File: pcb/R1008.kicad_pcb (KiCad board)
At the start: 2 copper layers, 45 x 33.3 mm, 9 parts, among them J1 PCIEXPRESS-X1, J2 CONN_R1000A_EXTENSION

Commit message: wip
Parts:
- removed G***: LOGO, pluggee:pluggee-LOGO-131X127
- removed G***: LOGO, pluggee:pluggee-QRNEG-085X085
- removed G***: LOGO, pluggee:pluggee-QRNEG-254X254
- removed MP1, MP2, MP3, MP4: ZIPTIE, Main:SLOT_ZIPTIE
- added C1: C0603, Main:CAPC0603, B.Cu at (128.2, 76.3)
- added C2: C0603, Main:CAPC0603, B.Cu at (148.2, 82.7)
- added C3: C0603, Main:CAPC0603, B.Cu at (148.2, 71.2)
- added C4: C0603, Main:CAPC0603, B.Cu at (148.2, 84.4)
- added C5: C0603, Main:CAPC0603, B.Cu at (148.2, 72.9)
- added C6: C0603, Main:CAPC0603, B.Cu at (145.0, 79.4)
- added C7: C0603, Main:CAPC0603, B.Cu at (145.0, 90.9)
- added J3: SOCKET254P-01X04-1725672, Main:SOCKET254P-01X04-1725672, B.Cu at (163.0, 76.0)
- added J4: CONN_01X03, Main:SOCKET254P-01X03, B.Cu at (152.5, 74.7)
- added J5: CONN_01X04, Main:SOCKET254P-01X04, B.Cu at (157.0, 76.0)
- added J6: CONN_01X03, Main:SOCKET254P-01X03, B.Cu at (152.5, 86.2)
- added J7: CONN_01X04, Main:SOCKET254P-01X04, B.Cu at (157.0, 87.5)
- added J8: CONN_01X03, Main:SOCKET254P-01X03, B.Cu at (131.3, 71.9)
- added R1: R0603, Main:RESC0603, B.Cu at (127.7, 92.4)
- added R10: R1206, Main:RESC1206, B.Cu at (148.2, 87.5)
- added R11: R0603, Main:RESC0603, B.Cu at (127.7, 89.0)
- added R12: R0603, Main:RESC0603, B.Cu at (127.7, 87.3)
- added R2: R0603, Main:RESC0603, B.Cu at (132.2, 92.4)
- added R3: R0603, Main:RESC0603, B.Cu at (132.2, 90.7)
- added R4: R0603, Main:RESC0603, B.Cu at (127.7, 90.7)
- added R5: R0603, Main:RESC0603, B.Cu at (127.7, 80.5)
- added R6: R0603, Main:RESC0603, B.Cu at (127.7, 82.2)
- added R7: R0603, Main:RESC0603, B.Cu at (127.7, 83.9)
- added R8: R0603, Main:RESC0603, B.Cu at (127.7, 85.6)
- added R9: R1206, Main:RESC1206, B.Cu at (148.2, 76.0)
- added U1: MAX31865AAP+, Main:SOP65P720X530X186-20, B.Cu at (141.5, 74.4)
- added U2: MAX31865AAP+, Main:SOP65P720X530X186-20, B.Cu at (141.5, 85.9)
- added U4: EFM8BB10F2G, Main:QFN50P300X300X75-20NT170X170, B.Cu at (132.7, 76.5)
- J2: value CONN_R1000A_EXTENSION -> SOCKET254P-01X04-1725672; footprint Main:CONN127P-02X10 -> Main:SOCKET254P-01X04-1725672
- moved J2 5.50 mm to (163.0, 87.5), turned to 90 degrees
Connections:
- J1 pad A18: ~MRESET -> /~MRESET~_CON
- J1 pad B18: C2D -> /C2D_CON
- J2 pad 1: ~MRESET -> /FORCE+_2
- J2 pad 2: C2D -> /RTDIN+_2
- J2 pad 3: SDA -> /RTDIN-_2
- J2 pad 4: SCLK -> /FORCE-_2
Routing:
- net PX1: track 46.9 -> 2.30 mm, vias 1 -> 0
- net PX2: track 45.2 -> 2.30 mm, vias 1 -> 0
- net PX3: track 43.5 -> 2.30 mm, vias 1 -> 0
- net PX4: track 41.9 -> 2.30 mm, vias 1 -> 0
- net ID0: track 38.5 -> 2.30 mm, vias 2 -> 0
- net ~MRESET: track 36.5 -> 1.08 mm, vias 1 -> 0
- net ID1: track 37.6 -> 2.30 mm, vias 2 -> 0
- net C2D: track 35.3 -> 0.21 mm
- net ID2: track 36.6 -> 2.30 mm, vias 2 -> 0
- net +3V3: track 42.9 -> 8.91 mm, vias 2 -> 0
- net RESERVED0: track 35.6 -> 2.30 mm, vias 2 -> 0
- net +5V: track 41.0 -> 8.91 mm, vias 1 -> 0
- net ID3: track 36.1 -> 4.60 mm, vias 2 -> 0
- net /MOSI: track 0.00 -> 28.6 mm, vias 0 -> 3
- net HT: track 49.4 -> 23.3 mm, vias 1 -> 0
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- added copper zone on B.Cu, net +3V3
- removed copper zone on B.Cu, net GND
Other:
- board text added: "R1008 v1.0.0 RTD Temperature Sensor plugg.ee Labs 12/2016 http://plugg.ee"
- board text removed: "R1005 v1.0.1 Breakout Board plugg.ee Labs 12/2016 http://plugg.ee"

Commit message: ready for release, gerbers updated
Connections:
- J1 pad B17: SCLK -> (no net)
- U1 pad 15: SCLK -> /SCLK
- U2 pad 15: SCLK -> /SCLK
- U4 pad 10: ID0 -> ID3
- U4 pad 2: SCLK -> /SCLK
- U4 pad 7: ID3 -> ID0
- U4 pad 8: ID2 -> ID1
- U4 pad 9: ID1 -> ID2
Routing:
- net ID0: track 2.30 -> 42.5 mm, vias 0 -> 2
- net ID2: track 2.30 -> 42.5 mm, vias 0 -> 2
- net ID1: track 2.30 -> 42.3 mm, vias 0 -> 2
- net ID3: track 4.60 -> 42.1 mm, vias 0 -> 2
- net GND: track 23.2 -> 56.0 mm, vias 1 -> 15
- net /RTDIN-_1: track 0.00 -> 32.1 mm, vias 0 -> 1
- net /RTDIN-_2: track 0.00 -> 30.4 mm, vias 0 -> 1
- net /FORCE-_1: track 0.00 -> 30.1 mm, vias 0 -> 1
- net SCLK: track 28.8 -> 0.00 mm, vias 3 -> 0
- net /SCLK: track 0.00 -> 28.8 mm, vias 0 -> 3
- net /FORCE-_2: track 0.04 -> 28.3 mm, vias 0 -> 1
- net ~MRESET: track 1.08 -> 26.1 mm, vias 0 -> 2
- net C2D: track 0.21 -> 25.1 mm, vias 0 -> 2
- net /FORCE+_2: track 0.00 -> 23.8 mm, vias 0 -> 1
- net /FORCE+_1: track 0.00 -> 23.4 mm, vias 0 -> 1
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- added copper zone on B.Cu, net GND
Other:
- board text added: "1F-"
- board text added: "1S+"
- board text added: "1S-"
- board text added: "2F+"
- board text added: "2F-"
- board text added: "2S+"
- board text added: "2S-"

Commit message: wip
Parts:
- removed J5, J7: CONN_01X04, Main:SOCKET254P-01X04
- removed J8: CONN_01X03, Main:SOCKET254P-01X03
- added TP1: TestPoint, Main:TestPoint000, F.Cu at (148.0, 91.3)
- added TP2: TestPoint, Main:TestPoint000, F.Cu at (162.3, 91.3)
- added TP3: TestPoint, Main:TestPoint000, F.Cu at (127.4, 91.3)
- added TP4: TestPoint, Main:TestPoint000, F.Cu at (130.3, 91.3)
- J2, J3: footprint Main:SOCKET254P-01X04-1725672 -> Main:70553-0038
- moved J3 5.00 mm to (167.0, 73.0), turned to 270 degrees
- moved J4 4.50 mm to (157.0, 74.7)
- moved J6 4.50 mm to (157.0, 86.2)
- moved J2 4.00 mm to (167.0, 87.5), turned to 270 degrees
- moved C2 3.80 mm to (152.0, 82.7)
- moved C3 3.80 mm to (152.0, 71.2)
- moved C4 3.80 mm to (152.0, 84.4)
- moved C5 3.80 mm to (152.0, 72.9)
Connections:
- J2 pad 1: /FORCE+_2 -> /FORCE-_2
- J2 pad 2: /RTDIN+_2 -> /RTDIN-_2
- J2 pad 3: /RTDIN-_2 -> /RTDIN+_2
- J2 pad 4: /FORCE-_2 -> /FORCE+_2
- J3 pad 1: /FORCE+_1 -> /FORCE-_1
- J3 pad 2: /RTDIN+_1 -> /RTDIN-_1
- J3 pad 3: /RTDIN-_1 -> /RTDIN+_1
- J3 pad 4: /FORCE-_1 -> /FORCE+_1
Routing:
- net /RTDIN+_1: track 20.5 -> 26.9 mm, vias 1 -> 2
- net /RTDIN-_1: track 32.1 -> 38.5 mm, vias 1 -> 2
- net /FORCE-_1: track 30.1 -> 35.3 mm, vias 1 -> 2
- net /RTDIN+_2: track 20.7 -> 25.5 mm
- net /FORCE2_2: track 13.6 -> 18.2 mm
- net /FORCE2_1: track 13.3 -> 17.8 mm
- net /FORCE+_1: track 23.4 -> 27.6 mm
- net /FORCE-_2: track 28.3 -> 32.2 mm
- net ~MRESET: track 26.1 -> 22.3 mm
- net /RTDIN-_2: track 30.4 -> 33.8 mm
- net /FORCE+_2: track 23.8 -> 26.8 mm, vias 1 -> 2
- net +3V3: track 8.91 -> 10.3 mm, vias 0 -> 1
- net GND: track 56.0 -> 57.2 mm
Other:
- board size 45 x 33.3 mm -> 51 x 36.3 mm
- board text added: "3.3V"
- board text added: "C2D"
- board text added: "GND"
- board text added: "~MRESET"

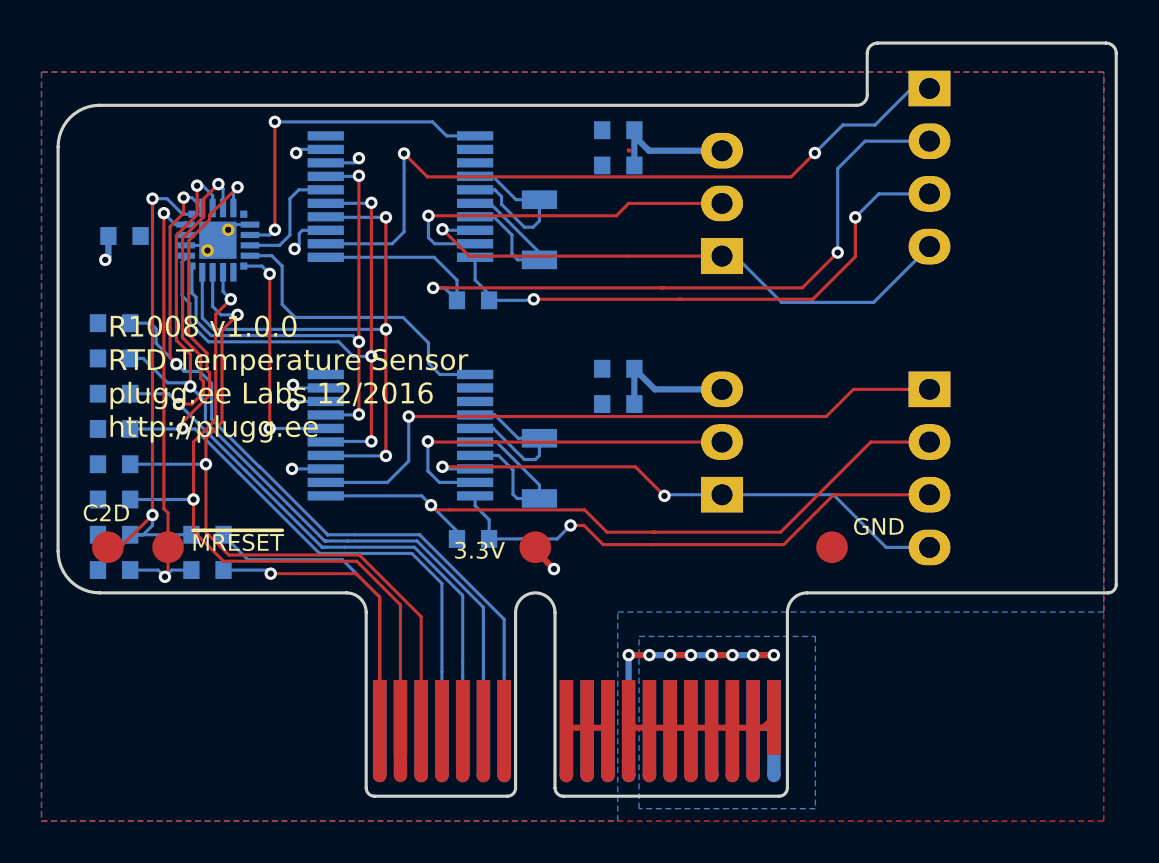
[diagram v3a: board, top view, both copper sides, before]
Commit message: added BOM, selected proper part for jumpers, added test points
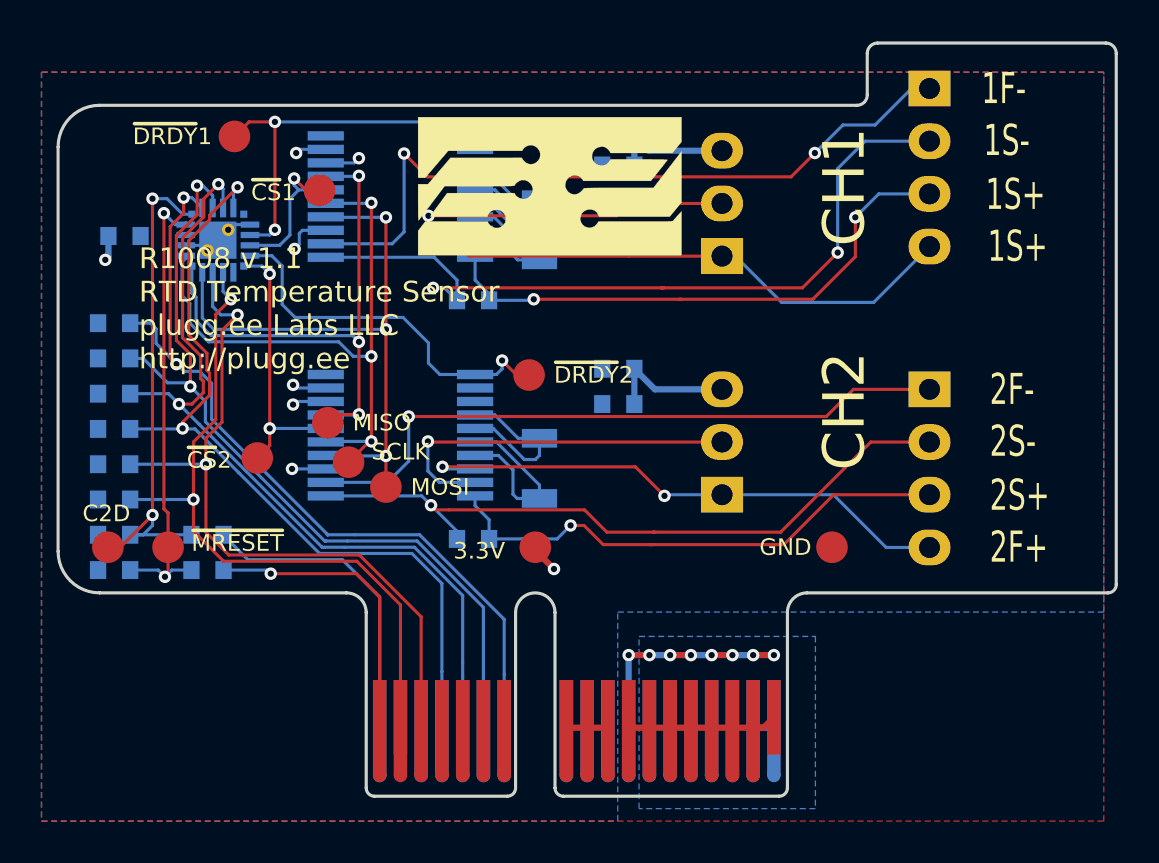
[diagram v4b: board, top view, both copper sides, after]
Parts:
- added A1: ART, pluggee:pluggeeLabsIcon-13X7, F.Cu at (148.7, 73.9)
- added TP10: TestPoint, Main:TestPoint000, F.Cu at (147.7, 83.0)
- added TP11: TestPoint, Main:TestPoint000, F.Cu at (134.6, 87.0)
- added TP5: TestPoint, Main:TestPoint000, F.Cu at (139.0, 87.2)
- added TP6: TestPoint, Main:TestPoint000, F.Cu at (133.5, 71.5)
- added TP7: TestPoint, Main:TestPoint000, F.Cu at (138.0, 85.3)
- added TP8: TestPoint, Main:TestPoint000, F.Cu at (137.6, 74.1)
- added TP9: TestPoint, Main:TestPoint000, F.Cu at (140.8, 88.4)
- C1, C2, C3, C4, C5, C6, C7: value C0603 -> CC0603KRX7R9BB104
- J4, J6: footprint Main:SOCKET254P-01X03 -> Main:CONN254P-01X03
- R1, R11, R12, R4, R5, R6, R7, R8: value R0603 -> RC0603FR-0710KL
- R10, R9: value R1206 -> RN732BTTD4000B25
- R2, R3: value R0603 -> RC0603FR-071KL
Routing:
- net /~DRDY~2: track 14.9 -> 18.3 mm, vias 0 -> 1
- net /~DRDY~1: track 16.4 -> 18.7 mm
- net /~CS~1: track 5.78 -> 7.89 mm, vias 0 -> 1
- net /~CS~2: track 11.6 -> 13.2 mm
- net /MISO: track 25.7 -> 27.4 mm
- net /SCLK: track 28.8 -> 30.3 mm
- net /MOSI: track 28.6 -> 30.1 mm
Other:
- board text added: "CH1"
- board text added: "CH2"
- board text added: "MISO"
- board text added: "MOSI"
- board text added: "R1008 v1.1 RTD Temperature Sensor plugg.ee Labs LLC http://plugg.ee"
- board text added: "SCLK"
- board text added: "~CS~1"
- board text added: "~CS~2"
- board text added: "~DRDY~1"
- board text added: "~DRDY~2"
- board text removed: "R1008 v1.0.0 RTD Temperature Sensor plugg.ee Labs 12/2016 http://plugg.ee"

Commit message: ready for v1.1.1 release
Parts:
- U4: value EFM8BB10F2G -> EFM8BB10F8G
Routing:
- net +3V3: track 10.3 -> 12.5 mm
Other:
- board text added: "1F+"
- board text added: "R1008 v1.1.1 RTD Temperature Sensor plugg.ee Labs LLC http://plugg.ee"
- board text removed: "R1008 v1.1 RTD Temperature Sensor plugg.ee Labs LLC http://plugg.ee"
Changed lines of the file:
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@@
     (thickness 1.6)
     (drawings 50)
-    (tracks 531)
+    (tracks 533)
     (zones 0)
     (modules 39)
@@
   (page A4)
   (layers
-    (0 F.Cu signal hide)
+    (0 F.Cu signal)
     (31 B.Cu signal hide)
     (32 B.Adhes user)
@@
   )
   (setup
-    (last_trace_width 0.15)
+    (last_trace_width 0.2)
     (user_trace_width 0.2)
     (user_trace_width 0.3)
     (trace_clearance 0.15)
-    (zone_clearance 0.508)
+    (zone_clearance 0.25)
     (zone_45_only yes)
     (trace_min 0.15)
@@
       (effects (font (size 0.7 0.7) (thickness 0.15)) (justify mirror))
     )
-    (fp_text value EFM8BB10F2G (at 0 -2.3) (layer B.Fab) hide
+    (fp_text value EFM8BB10F8G (at 0 -2.3) (layer B.Fab) hide
       (effects (font (size 0.127 0.127) (thickness 0.03175)) (justify mirror))
     )
@@
     (effects (font (size 1.5 1) (thickness 0.2)) (justify left))
   )
-  (gr_text 1S+ (at 169.8 76.8) (layer F.SilkS)
+  (gr_text 1F+ (at 169.8 76.8) (layer F.SilkS)
     (effects (font (size 1.5 1) (thickness 0.2)) (justify left))
   )
@@
     (effects (font (size 1.5 1) (thickness 0.2)) (justify left))
   )
-  (gr_text "R1008 v1.1\nRTD Temperature Sensor\nplugg.ee Labs LLC\nhttp://plugg.ee" (at 128.9 79.8) (layer F.SilkS)
+  (gr_text "R1008 v1.1.1\nRTD Temperature Sensor\nplugg.ee Labs LLC\nhttp://plugg.ee" (at 128.9 79.8) (layer F.SilkS)
     (effects (font (size 1 1) (thickness 0.2)) (justify left))
   )
@@
   (segment (start 153.50012 102.30124) (end 153.50012 100) (width 0.15) (layer B.Cu) (net 2))
   (segment (start 152.49936 102.30124) (end 152.49936 100) (width 0.15) (layer B.Cu) (net 2))
+  (segment (start 131.15 76.25) (end 129.0245 76.25) (width 0.2) (layer B.Cu) (net 3))
+  (segment (start 129.0245 76.25) (end 128.9745 76.3) (width 0.2) (layer B.Cu) (net 3))
   (segment (start 148 91.3) (end 148 91.45) (width 0.3) (layer F.Cu) (net 3))
   (segment (start 148 91.45) (end 148.9 92.35) (width 0.3) (layer F.Cu) (net 3))
@@
   )
   (zone (net 3) (net_name +3V3) (layer B.Cu) (hatch edge 0.508)
-    (connect_pads (clearance 0.22))
+    (connect_pads (clearance 0.25))
     (min_thickness 0.2)
     (fill yes (arc_segments 16) (thermal_gap 0) (thermal_bridge_width 0.25))
@@
   )
   (zone (net 2) (net_name GND) (layer F.Cu) (hatch edge 0.508)
-    (connect_pads (clearance 0.22))
+    (connect_pads (clearance 0.25))
     (min_thickness 0.2)
     (fill yes (arc_segments 16) (thermal_gap 0) (thermal_bridge_width 0.25))
